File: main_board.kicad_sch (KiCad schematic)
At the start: 90 parts, among them CN10 DF40C-40DP-0.4V, CN11 DF40C-30DP-0.4V, CN19 DF40C-24DP-0.4V, CN2 DF40C-50DP-0.4V, CN8 DF40C-40DP-0.4V, J4 DF40C-100DP-0.4V51, J5 DF40C-100DP-0.4V51, Q4 MMBT3904-C20526, SW1 RESET_L, SW2 PWRON_L, U11 SiP32508DT, U47 ES8388, U48 TS5A23157DGSR, U49 TS5A23157DGSR, U50 PAM8302AASCR, U51 PAM8302AASCR, U52 TPS7A0233PDBVR, U62 PCA9306DCUR, U63 AP2120N-2.8TRG1, U66 DF40B-10DS-0.4V, U67 SIP32508DT-T1-GE3, U68 SN74AHCT125PWR, U8 ESD7104MUTAG_C2987068

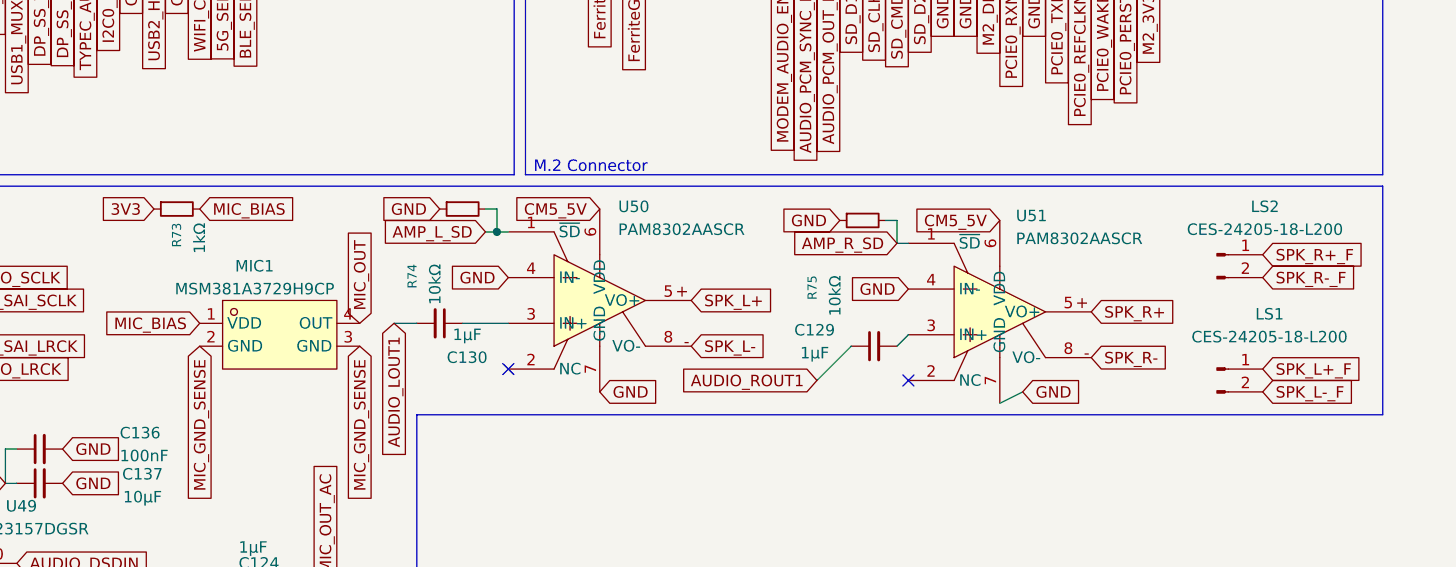
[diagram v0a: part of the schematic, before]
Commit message: finished BOM, replaced discontinued parts, added missing footprints, updated schematics and libraries
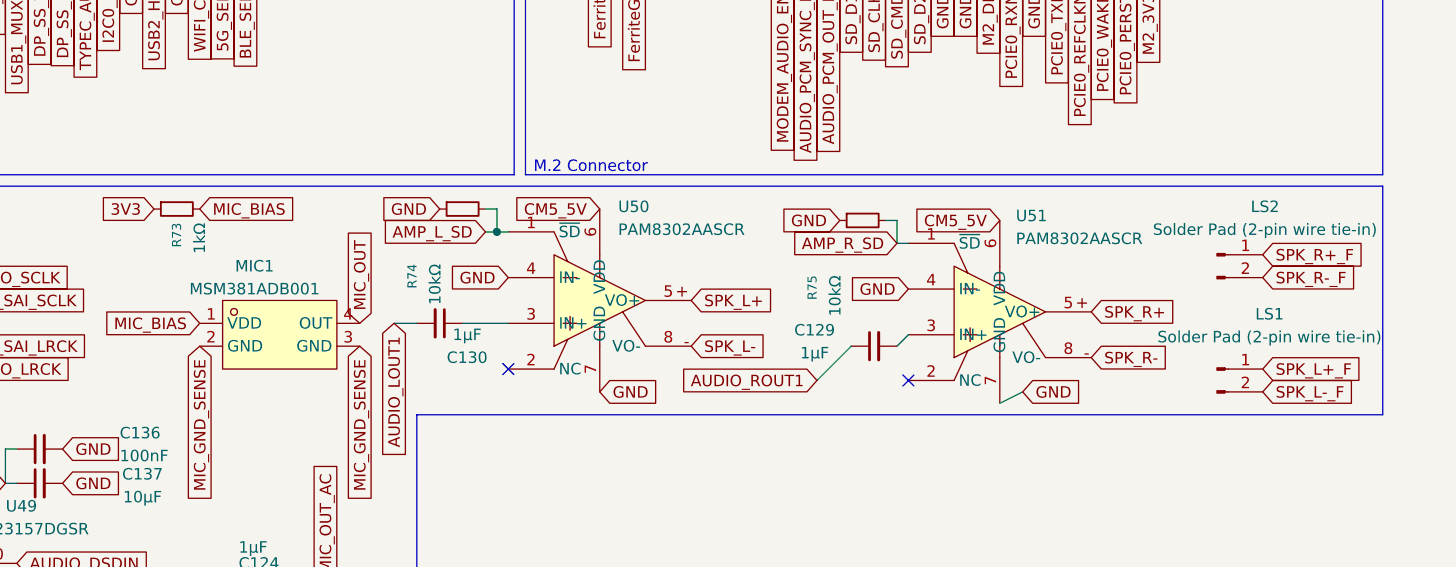
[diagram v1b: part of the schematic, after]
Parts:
- C111, C114, C115, C133, C134, C136, C139, C147, C21, C211, C215, C219: LCSC Part (none) -> C1591
- C116, C131, C135, C137, C140: LCSC Part (none) -> C380317; MPN CL10A106KP8NNNC -> TCC0603X5R106M160CT
- C117, C123, C19: LCSC Part (none) -> C23630; MPN CL10B225KA8NNNC -> CL10A225KO8NNNC
- C118, C120, C121, C124, C129, C130, C132, C138, C150, C155: LCSC Part (none) -> C15849; MPN CL10B105KA8NNNC -> CL10A105KB8NNNC
- C119, C122, C156: LCSC Part (none) -> C14858
- C125, C126, C127, C128: LCSC Part (none) -> C100040; MPN CL10B102KB8NNNC -> CC0603KRX7R9BB102
- C213: footprint (none) -> Capacitor_SMD:C_0805_2012Metric; LCSC Part (none) -> C16780; MPN (none) -> CL21A476MQYNNNE
- C217: LCSC Part (none) -> C49326377; MPN CL10B475KA8NNNC -> 0603X5R475K160NT
- FB2: LCSC Part (none) -> C107335; MPN (none) -> MPZ1608S601ATA00; Manufacturer (none) -> TDK
- FB6, FB7, FB8, FB9: footprint (none) -> Inductor_SMD:L_0603_1608Metric; LCSC Part (none) -> C107335; MPN (none) -> MPZ1608S601ATA00; Manufacturer (none) -> TDK
- J4: footprint CONN100_DF40C-100DP-0.4V51_HIR -> slate113:CONN100_DF40C-100DP-0.4V51_HIR; LCSC Part (none) -> C531031; MPN DF40C-100DP-0.4V51 -> DF40C-100DP-0.4V(51)
- J5: footprint CONN100_DF40C-100DP-0.4V51_HIR -> slate113:CONN100_DF40C-100DP-0.4V51_HIR; LCSC Part (none) -> C531031; MPN (none) -> DF40C-100DP-0.4V(51)
- LS1, LS2: value CES-24205-18-L200 -> Solder Pad (2-pin wire tie-in); footprint (none) -> TestPoint:TestPoint_Pad_D2.0mm
- MIC1: value MSM381A3729H9CP -> MSM381ADB001; footprint slate113:MIC-SMD_4P-L3.8-W3.0-P2.46-S1.70-TR -> (none); LCSC Part C966940 -> C5375366; MPN MSM381A3729H9CP -> MSM381ADB001
- R100, R108, R109, R74, R75, R96: LCSC Part (none) -> C25804; MPN RC0603FR-0710KL -> 0603WAF1002T5E
- R105, R17: LCSC Part (none) -> C25803; MPN RC0603FR-07100KL -> 0603WAF1003T5E
- R106, R107: LCSC Part (none) -> C23204; MPN RC0603FR-07560RL -> 0603WAF5600T5E
- R67: LCSC Part (none) -> C23140; MPN RC0603FR-0733RL -> 0603WAF330JT5E
- R70: LCSC Part (none) -> C22859; MPN RC0603FR-0710RL -> 0603WAF100JT5E
- R71, R72, R73: LCSC Part (none) -> C21190; MPN RC0603FR-071KL -> 0603WAF1001T5E
- R97, R98: LCSC Part (none) -> C23162; MPN RC0603FR-074K7L -> 0603WAF4701T5E
- R99: LCSC Part (none) -> C25811; MPN RC0603FR-07200KL -> 0603WAF2003T5E
- SW1: DigiKey Part (none) -> 108-KMR231GLFSTR-ND; LCSC Part (none) -> C99271; MPN C&K KMR231GLFS -> KMR231G LFS
- SW2: DigiKey Part (none) -> 108-KMR231GLFSTR-ND; LCSC Part (none) -> C99271; MPN C&K KMR231GLFS -> KMR231G LFS; Manufacturer DigiKey -> C&K
- U11: LCSC Part (none) -> C139515; MPN SiP32508DT -> SIP32508DT-T1-GE3

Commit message: imported footprints and 3d models, replaced obsolete components, finished schematic audit, wired new usb hub and flash chip + more, removed stale nets
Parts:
- removed MIC1: MSM381ADB001, symbol slate113:MSM381A3729H9CP
- added C59: 100nF, Capacitor_SMD:C_0603_1608Metric, symbol Device:C_Small
- added R121, R122, R123, R125, R126, R127, R128, R129: 10kΩ, Resistor_SMD:R_0603_1608Metric, symbol Device:R_Small
- added R124: 10kΩ, symbol Device:R_Small
- added U65: MSM381ADB001, slate113:MIC-SMD_5P_L3.5-W2.7-P0.82_MSM381ADB001, symbol slate113:MSM381ADB001
- added U69: TCA9535PWR, slate113:TSSOP-24_L7.8-W4.4-P0.65-LS6.4-BL, symbol slate113:TCA9535PWR_C130204
- C118, C120, C121, C124, C129, C130, C132, C138, C150, C155: LCSC Part C15849 -> C92848; MPN CL10A105KB8NNNC -> UMK107BJ105KA-T; Manufacturer Samsung Electro-Mechanics -> Taiyo Yuden
- C217: LCSC Part C49326377 -> C77045; MPN 0603X5R475K160NT -> GRM188R61C475KE11D; Manufacturer Samsung Electro-Mechanics -> Murata Electronics
- FB2: footprint (none) -> Inductor_SMD:L_0603_1608Metric
- LS1, LS2: value Solder Pad (2-pin wire tie-in) -> Solder Pad
- R100, R108, R109, R74, R75, R96: LCSC Part C25804 -> C840630; MPN 0603WAF1002T5E -> CR0603-FX-1002ELF; Manufacturer Yageo -> Bourns
- R70: LCSC Part C22859 -> C109318; MPN 0603WAF100JT5E -> RC0603FR-0710RL
- R71, R72, R73: LCSC Part C21190 -> C118155; MPN 0603WAF1001T5E -> ERJ3EKF1001V; Manufacturer Yageo -> Panasonic
- R97, R98: LCSC Part C23162 -> C163914; MPN 0603WAF4701T5E -> WR06X4701FTL; Manufacturer Yageo -> Walsin
- R99: LCSC Part C25811 -> C118142; MPN 0603WAF2003T5E -> ERJ3EKF2003V; Manufacturer Yageo -> Panasonic
- SW1: value RESET_L -> SW_Push; DigiKey Part 108-KMR231GLFSTR-ND -> (none); MPN KMR231G LFS -> KMR231GLFS
- SW2: value PWRON_L -> SW_Push; DigiKey Part 108-KMR231GLFSTR-ND -> (none); MPN KMR231G LFS -> KMR231GLFS
- U68: DigiKey Part (none) -> 1727-6305-1-ND
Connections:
- net 3V3: now also C59.2, R124.2, U69.24 (VCC)
- net AMP_L_SD: now also U69.8 (P04); no longer J4.80
- net AMP_R_SD: now also U69.9 (P05); no longer J4.82
- net GND: now also C59.1, R121.1, R122.1, R123.1, R125.1, R126.1, R127.1, R128.1, R129.1, U65.2 (GND), U65.3 (GND), U65.4 (GND), U69.12 (GND), U69.2 (A1), U69.21 (A0), U69.3 (A2); no longer CN19.16, CN19.18
- net I2C0_SCL: now also U69.22 (SCL)
- net I2C0_SDA: now also U69.23 (SDA)
- net MIC_BIAS: now also U65.5 (VDD)
- net MIC_OUT: now also U65.1 (OUT)
- net MODEM_AUDIO_EN: now also U69.11 (P07); no longer J4.91
- net PCIE0_WAKE: now also CN10.35
- net RADIO_EN: now also U69.10 (P06); no longer J4.89
- net USB_HUB_EN: now reaches CN2.18
- net USB_HUB_EN: now also J4.37, R124.1
- net BT_EN: now reaches CN2.19
- net BT_EN: now also U69.4 (P00)
- net WIFI_EN: now reaches CN2.20
- net WIFI_EN: now also U69.6 (P02)
- net WOWLAN: now reaches CN2.21
- net WOWLAN: now also U69.5 (P01)
- net COMBO_EN: now reaches CN2.22
- net COMBO_EN: now also U69.7 (P03)
- net MODEM_W_DISABLE: now reaches CN10.36
- net MIC_GND_SENSE: no longer names the net of C119.1, U47.23 (RIN1)
- net RP_RST renamed ESP_RST
- new net RF_V1: CN19.16, U69.20 (P17)
- new net RF_V2: CN19.18, U69.19 (P16)
- new net R_UNUSED: R121.2, R122.2, R123.2, R125.2, R126.2, R127.2, R128.2, R129.2, U69.13 (P10), U69.14 (P11), U69.15 (P12), U69.16 (P13), U69.17 (P14), U69.18 (P15)
- no-connect marks 97 -> 90
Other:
- note added: "GPIO Expander"
- note added: "Random Resistor"
- note added: "Resistors"
- moved on the sheet: C111, C114, C115, C116, C117, C118, C119, C120, C121, C122, C123, C124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

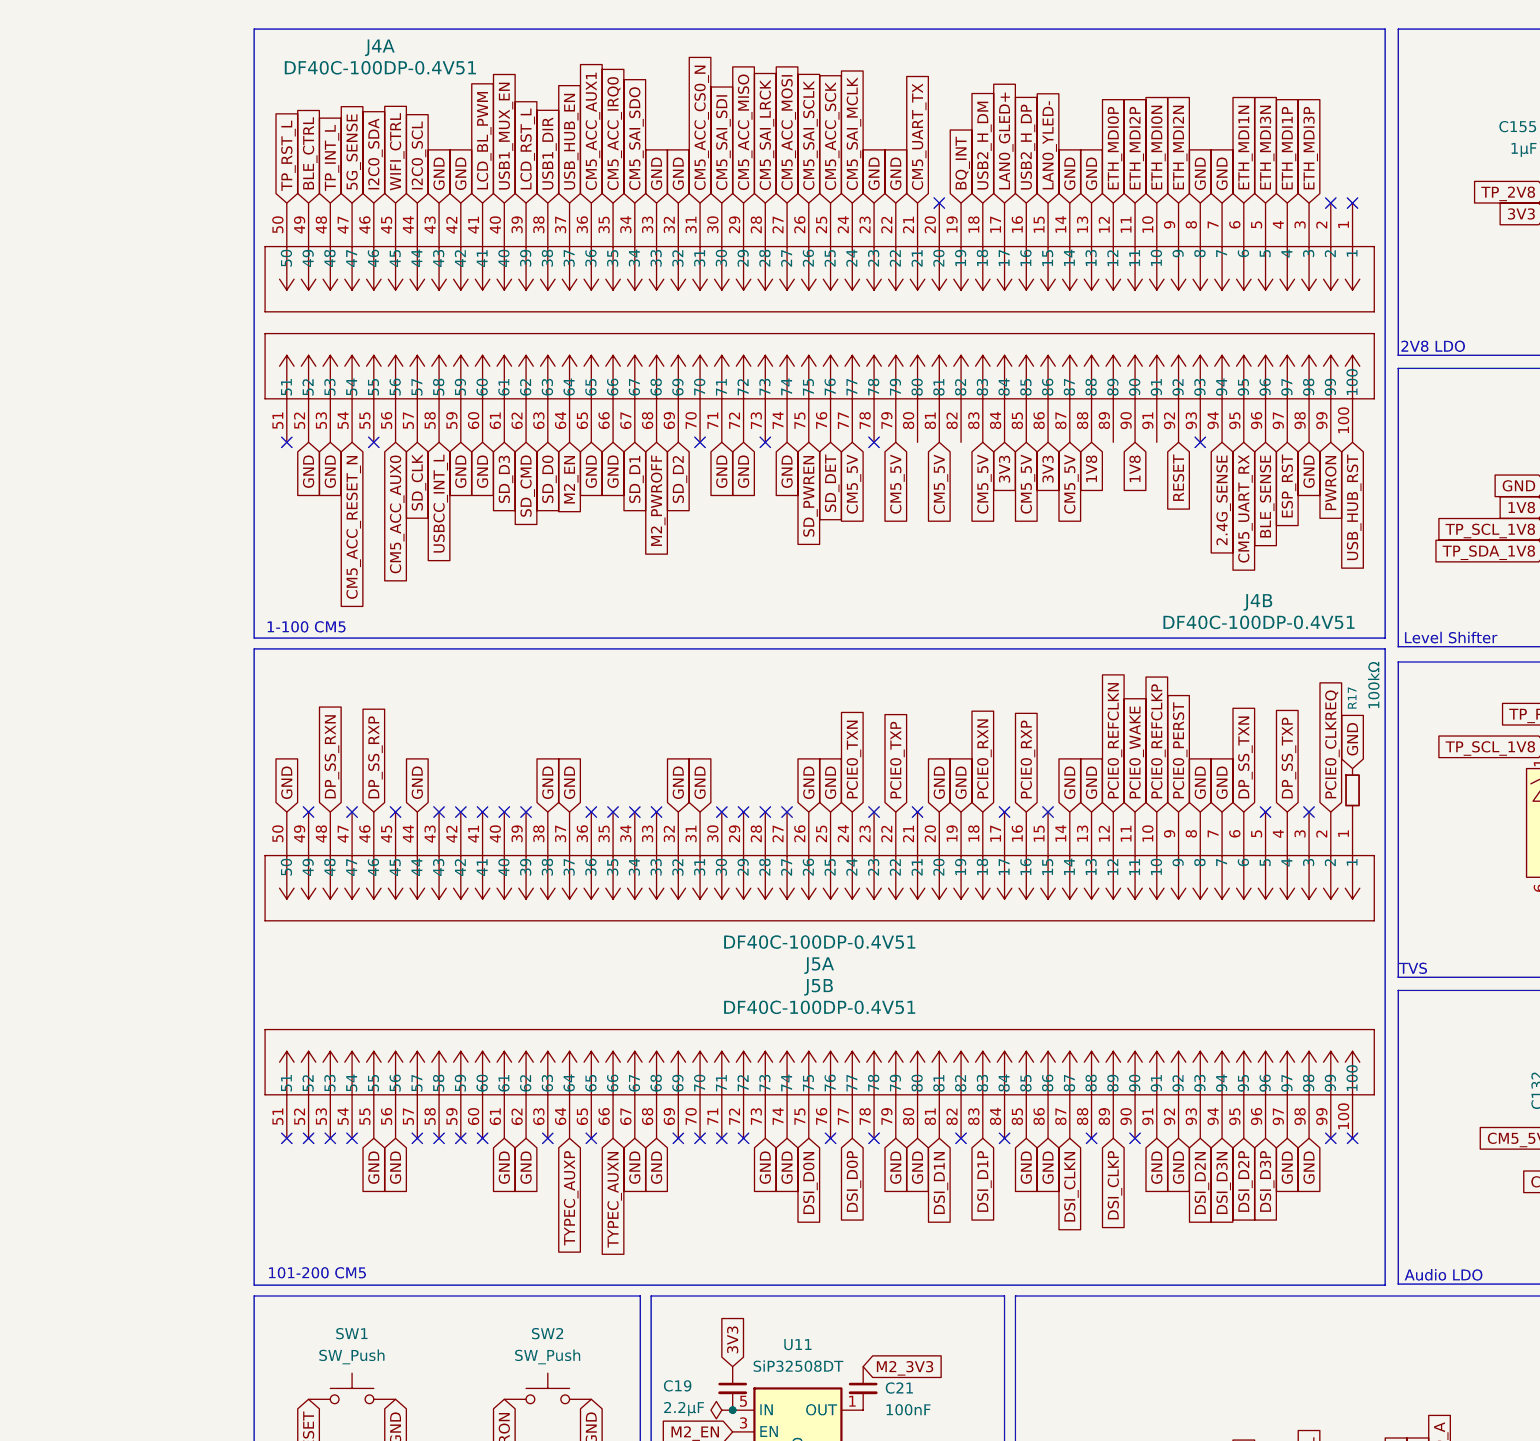
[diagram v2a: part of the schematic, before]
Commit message: configured 8-layer pcb with micro vias, finished power mezzanine routing, completed io port, started work on slateconnect mezzanine
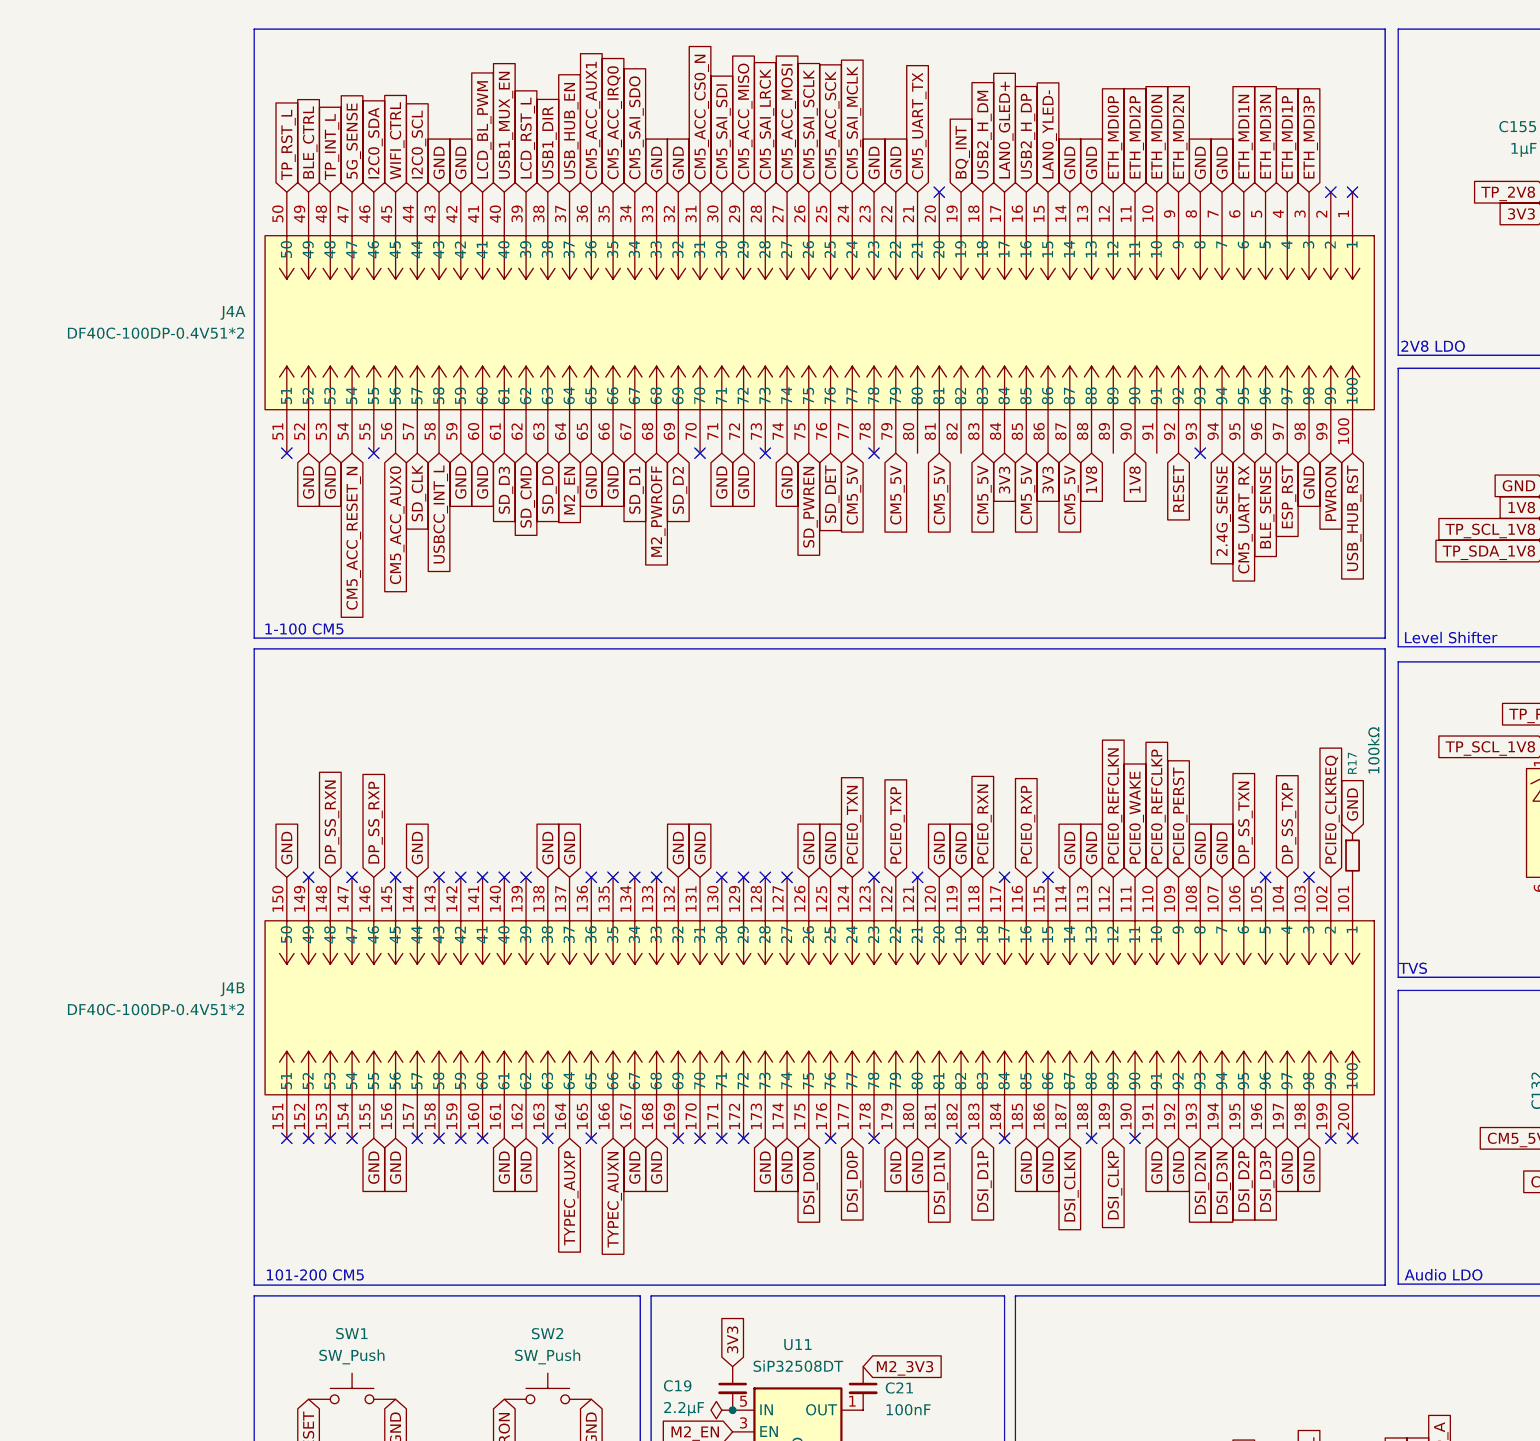
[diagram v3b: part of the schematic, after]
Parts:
- removed J4, J5: DF40C-100DP-0.4V51, slate113:CONN100_DF40C-100DP-0.4V51_HIR, symbol slate113:DF40C-100DP-0.4V51
- added J4: DF40C-100DP-0.4V51*2, slate113:Raspberry-Pi-4-Compute-Module, symbol slate113:CM5_|_DF40C-100DP-0.4V51_*2
- LS1, LS2: footprint TestPoint:TestPoint_Pad_D2.0mm -> TestPoint:TestPoint_2Pads_Pitch2.54mm_Drill0.8mm
- R124: footprint (none) -> Resistor_SMD:R_0603_1608Metric
- SW1, SW2: footprint (none) -> slate113:KEY-SMD_KMR2XXGXXX
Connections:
- net 1V8: now also J4.88, J4.90
- net 2.4G_SENSE: now also J4.94
- net 3V3: now also J4.84, J4.86
- net 5G_SENSE: now also J4.47
- net BLE_CTRL: now also J4.49
- net BLE_SENSE: now also J4.96
- net BQ_INT: now also J4.19
- net CM5_5V: now also J4.77, J4.79, J4.81, J4.83, J4.85, J4.87
- net CM5_ACC_AUX0: now also J4.56
- net CM5_ACC_AUX1: now also J4.36
- net CM5_ACC_CS0_N: now also J4.31
- net CM5_ACC_IRQ0: now also J4.35
- net CM5_ACC_MISO: now also J4.29
- net CM5_ACC_MOSI: now also J4.27
- net CM5_ACC_RESET_N: now also J4.54
- net CM5_ACC_SCK: now also J4.25
- net CM5_SAI_LRCK: now also J4.28
- net CM5_SAI_MCLK: now also J4.24
- net CM5_SAI_SCLK: now also J4.26
- net CM5_SAI_SDI: now also J4.30
- net CM5_SAI_SDO: now also J4.34
- net CM5_UART_RX: now also J4.95
- net CM5_UART_TX: now also J4.21
- net DP_SS_RXN: now also J4.148 (48)
- net DP_SS_RXP: now also J4.146 (46)
- net DP_SS_TXN: now also J4.106 (6)
- net DP_SS_TXP: now also J4.104 (4)
- net DSI_CLKN: now also J4.187 (87)
- net DSI_CLKP: now also J4.189 (89)
- net DSI_D0N: now also J4.175 (75)
- net DSI_D0P: now also J4.177 (77)
- net DSI_D1N: now also J4.181 (81)
- net DSI_D1P: now also J4.183 (83)
- net DSI_D2N: now also J4.193 (93)
- net DSI_D2P: now also J4.195 (95)
- net DSI_D3N: now also J4.194 (94)
- net DSI_D3P: now also J4.196 (96)
- net ESP_RST: now also J4.97
- net ETH_MDI0N: now also J4.10
- net ETH_MDI0P: now also J4.12
- net ETH_MDI1N: now also J4.6
- net ETH_MDI1P: now also J4.4
- net ETH_MDI2N: now also J4.9
- net ETH_MDI2P: now also J4.11
- net ETH_MDI3N: now also J4.5
- net ETH_MDI3P: now also J4.3
- net GND: now also J4.107 (7), J4.108 (8), J4.113 (13), J4.114 (14), J4.119 (19), J4.120 (20), J4.125 (25), J4.126 (26), J4.13, J4.131 (31), J4.132 (32), J4.137 (37), J4.138 (38), J4.14, J4.144 (44), J4.150 (50), J4.155 (55), J4.156 (56), J4.161 (61), J4.162 (62), J4.167 (67), J4.168 (68), J4.173 (73), J4.174 (74), J4.179 (79), J4.180 (80), J4.185 (85), J4.186 (86), J4.191 (91), J4.192 (92), J4.197 (97), J4.198 (98), J4.22, J4.23, J4.32, J4.33, J4.42, J4.43, J4.52, J4.53, J4.59, J4.60, J4.65, J4.66, J4.7, J4.71, J4.72, J4.74, J4.8, J4.98
- net I2C0_SCL: now also J4.44
- net I2C0_SDA: now also J4.46
- net LAN0_GLED+: now also J4.17
- net LAN0_YLED-: now also J4.15
- net LCD_BL_PWM: now also J4.41
- net LCD_RST_L: now also J4.39
- net M2_EN: now also J4.64
- net M2_PWROFF: now also J4.68
- net PCIE0_CLKREQ: now also J4.102 (2)
- net PCIE0_PERST: now also J4.109 (9)
- net PCIE0_REFCLKN: now also J4.112 (12)
- net PCIE0_REFCLKP: now also J4.110 (10)
- net PCIE0_RXN: now also J4.118 (18)
- net PCIE0_RXP: now also J4.116 (16)
- net PCIE0_TXN: now also J4.124 (24)
- net PCIE0_TXP: now also J4.122 (22)
- net PCIE0_WAKE: now also J4.111 (11)
- net PWRON: now also J4.99
- net RESET: now also J4.92
- net SD_CLK: now also J4.57
- net SD_CMD: now also J4.62
- net SD_D0: now also J4.63
- net SD_D1: now also J4.67
- net SD_D2: now also J4.69
- net SD_D3: now also J4.61
- net SD_DET: now also J4.76
- net SD_PWREN: now also J4.75
- net TP_INT_L: now also J4.48
- net TP_RST_L: now also J4.50
- net TYPEC_AUXN: now also J4.166 (66)
- net TYPEC_AUXP: now also J4.164 (64)
- net USB1_DIR: now also J4.38
- net USB1_MUX_EN: now also J4.40
- net USB2_H_DM: now also J4.18
- net USB2_H_DP: now also J4.16
- net USBCC_INT_L: now also J4.58
- net USB_HUB_EN: now also J4.37
- net USB_HUB_RST: now also J4.100
- net WIFI_CTRL: now also J4.45
- net at R17.2: now also J4.101 (1)
